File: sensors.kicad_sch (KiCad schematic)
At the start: 13 parts, among them U11 LPS22DF, U4 LSM6DSV80XTR, U5 LSM6DSV80XTR, U8 LIS2MDL

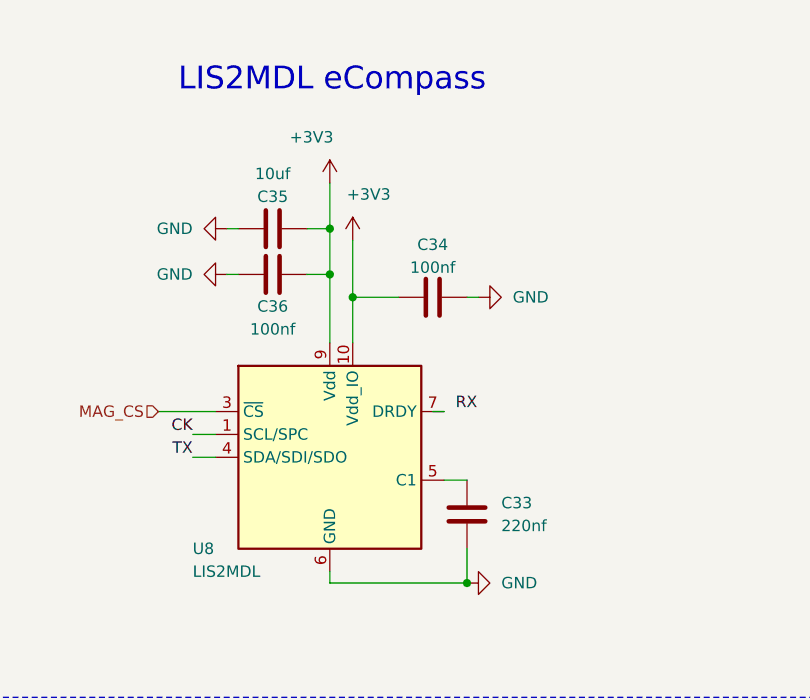
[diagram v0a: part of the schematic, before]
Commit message: 10/01/2025
1v1 fix and v regulator final decision, general BOM corrections and allignments
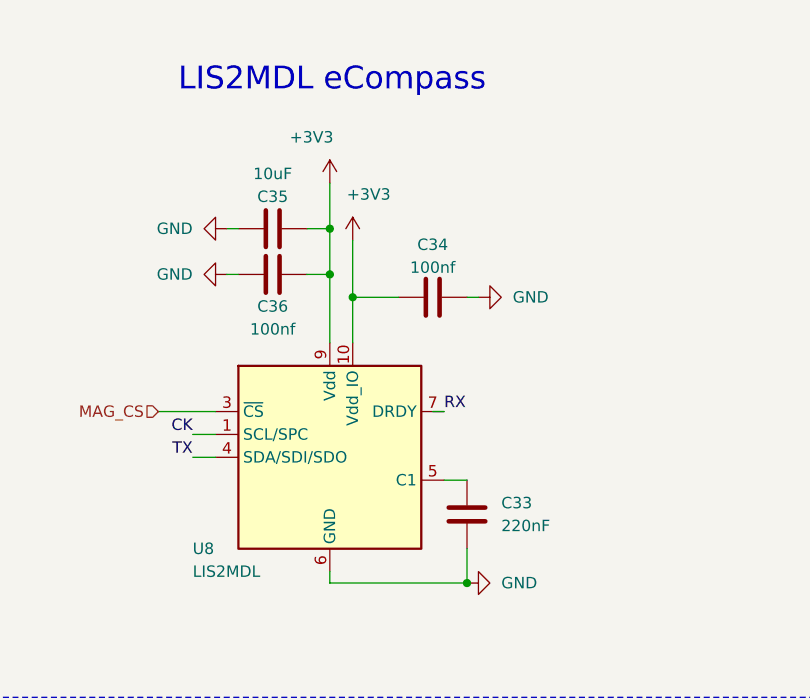
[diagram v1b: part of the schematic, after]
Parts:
- C33: value 220nf -> 220nF
- C35: value 10uf -> 10uF
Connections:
- net RX: now also U8.7 (DRDY)
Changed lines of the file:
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@@
 	)
 	(label "RX"
-		(at 223.52 127 0)
+		(at 222.25 127 0)
 		(effects
 			(font
@@
 			)
 		)
-		(property "Value" "220nf"
+		(property "Value" "220nF"
 			(at 228.6 139.6999 0)
 			(effects
@@
 			)
 		)
-		(property "Value" "10uf"
+		(property "Value" "10uF"
 			(at 203.2 100.584 90)
 			(effects
